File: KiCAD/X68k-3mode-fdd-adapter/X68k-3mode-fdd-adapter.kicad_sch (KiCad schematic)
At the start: 49 parts, among them J1 Conn_02x17_Odd_Even, J2 Double Row 3A Copper Alloy 34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, J3 Conn_01x04, J4 PH-4A, J5 SDIO, J6 Conn_01x04, J7 Conn_01x03_Pin, P1 USB_C_Plug_USB2.0, Q1 2SC2712, SW1 SW_DIP_x02, SW2 SW_SPDT, U1 CH32V003F4U6, U4 74HC153, U5 74HC153, U6 ULN2003A

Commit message: Minyas-XのV2基板の回路図を一通り日いいたので一旦コミット
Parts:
- removed C1: 10uF, Capacitor_SMD:C_0603_1608Metric, symbol Device:C_Small
- removed C2, C3, C4: 0.1uF, Capacitor_SMD:C_0603_1608Metric, symbol Device:C_Small
- removed D1, D2: SK6812MINI, x68k-lib:SK6812MINI-HS, symbol X68k-lib:SK6812MINI-HS
- removed J2: Double Row 3A Copper Alloy 34P Female Headers (PM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, x68k-lib:PinSocket_2x17_P2.54mm_Horizontal_Mirror, symbol Connector_Generic:Conn_02x17_Odd_Even
- removed J3: Conn_01x04, x68k-lib:TE_AMP_171826-4, symbol Connector_Generic:Conn_01x04
- removed J5: SDIO, Connector_PinHeader_2.54mm:PinHeader_1x02_P2.54mm_Vertical, symbol Connector:Conn_01x02_Pin
- removed J7: Conn_01x03_Pin, Connector_PinHeader_2.54mm:PinHeader_1x03_P2.54mm_Vertical, symbol Connector:Conn_01x03_Pin
- removed P1: USB_C_Plug_USB2.0, Connector_USB:USB_C_Receptacle_GCT_USB4125-xx-x-0190_6P_TopMnt_Horizontal, symbol Connector:USB_C_Receptacle_PowerOnly_6P
- removed R0, R1, R10, R11, R12, R13, R2, R3, R5, R6, R7: 1K, Resistor_SMD:R_0603_1608Metric, symbol Device:R_Small_US
- removed R24, R25, R26, R27: 10K, Resistor_SMD:R_0603_1608Metric, symbol Device:R_Small_US
- removed R31, R32: 5.1k, Resistor_SMD:R_0603_1608Metric, symbol Device:R_Small_US
- removed SW2: SW_SPDT, Connector_PinHeader_2.54mm:PinHeader_1x03_P2.54mm_Vertical, symbol Switch:SW_SPDT
- removed TP2, TP4: TestPoint, TestPoint:TestPoint_Pad_1.0x1.0mm, symbol Connector:TestPoint
- removed U1: CH32V003F4U6, Package_DFN_QFN:QFN-20-1EP_3x3mm_P0.4mm_EP1.65x1.65mm_ThermalVias, symbol X68k-lib:CH32V003F4U6
- removed U4, U5: 74HC153, Package_SO:SO-16_5.3x10.2mm_P1.27mm, symbol 74xx_IEEE:74153
- removed U6: ULN2003A, Package_SO:SOP-16_3.9x9.9mm_P1.27mm, symbol Transistor_Array:ULN2003A
- added C101: 0.1uF, symbol Device:C_Small
- added C103, C104, C105, C106, C107: 0.1uF, Capacitor_SMD:C_0603_1608Metric, symbol Device:C_Small
- added J103, J104: Conn_01x02, symbol Connector_Generic:Conn_01x02
- added J106, J109: Conn_02x17_Odd_Even, symbol Connector_Generic:Conn_02x17_Odd_Even
- added JP101: Jumper_NC_Small, Jumper:SolderJumper-2_P1.3mm_Bridged_RoundedPad1.0x1.5mm, symbol device:Jumper_NC_Small
- added JP102, JP103: Jumper_2_Small_Open, symbol Jumper:Jumper_2_Small_Open
- added Q101: DTC143Z, symbol Transistor_BJT:DTC143Z
- added R101, R104: R100 (0.1Ω), Resistor_SMD:R_2512_6332Metric_Pad1.40x3.35mm_HandSolder, symbol Device:R_Small_US
- added R113, R114: 2.2k, symbol Device:R_Small_US
- added R115: 1k, symbol Device:R_Small_US
- added R120, R121, R122, R123, R124, R125, R126, R127, R128, R129, R130, R131, R132, R133, R134, R135, R136, R137: 1K, Resistor_SMD:R_0603_1608Metric, symbol Device:R_Small_US
- added RP101: 4.7k, Resistor_SMD:R_Array_Convex_4x0603, symbol device:R_PACK4
- added SW102: RESET_SW, symbol Switch:SW_Push
- added TP104, TP105, TP106, TP108, TP109, TP110, TP111, TP113, TP114: TestPoint, TestPoint:TestPoint_Pad_1.0x1.0mm, symbol Connector:TestPoint
- added U101: INA3221AIRGVR, Housings_DFN_QFN:QFN-16-1EP_4x4mm_Pitch0.65mm, symbol x68000-ext:INA3221
- added U102, U104, U105: SLG46826G(V2), Package_SO:TSSOP-20_4.4x6.5mm_P0.65mm, symbol X68k-lib:SLG46826G(V2)
- added U103: CH32X035C8T6, Package_LQFP:LQFP-48-1EP_7x7mm_P0.5mm, symbol X68k-lib:CH32X035C8T6
- J102: renamed from J4; value PH-4A -> 4pin
- renumbered BZ1 to BZ101, C5 to C102, D3 to D103, H1 to H101, J6 to J105, J1 to J107, Q1 to Q102, R21 to R102, R20 to R103, R22 to R119, SW1 to SW101, TP3 to TP101, TP1 to TP102
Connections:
- net +5V: no longer C102.1, J102.1 (Pin_1)
- net BUZZER: now also U103.17 (PA7)
- net DIPSW_0: now also U103.40 (PA8)
- net DIPSW_1: now also U103.41 (PA9)
- net DIRECTION: now also R129.2, U103.45 (PA13)
- net DISK_CHANGE_DOSV: now also J106.34 (Pin_34), J109.34 (Pin_34), U103.28 (PB8)
- net DISK_IN: now also U104.5 (IO10)
- net DISK_TYPE_SELECT: no longer TP101.1
- net DRIVE_SELECT_0: now also R120.2, U102.1 (IO14)
- net DRIVE_SELECT_1: now also R121.2, U102.2 (IO13)
- net DRIVE_SELECT_2: now also R122.2, U102.3 (IO12)
- net DRIVE_SELECT_3: now also R123.2, U102.4 (IO11)
- net EJECT: now also R133.2, U103.2 (PA16)
- net EJECT_MASK: now also R134.2, U103.3 (PA17)
- net ERR_DISK: now also U104.6 (IO9)
- net GND: now also C101.2, C103.2, C104.2, C105.2, C106.2, C107.2, J103.2 (Pin_2), J104.2 (Pin_2), J106.11 (Pin_11), J106.13 (Pin_13), J106.15 (Pin_15), J106.17 (Pin_17), J106.19 (Pin_19), J106.21 (Pin_21), J106.23 (Pin_23), J106.25 (Pin_25), J106.27 (Pin_27), J106.29 (Pin_29), J106.31 (Pin_31), J106.33 (Pin_33), J106.5 (Pin_5), J106.7 (Pin_7), J106.9 (Pin_9), J109.11 (Pin_11), J109.13 (Pin_13), J109.15 (Pin_15), J109.17 (Pin_17), J109.19 (Pin_19), J109.21 (Pin_21), J109.23 (Pin_23), J109.25 (Pin_25), J109.27 (Pin_27), J109.29 (Pin_29), J109.31 (Pin_31), J109.33 (Pin_33), J109.5 (Pin_5), J109.7 (Pin_7), J109.9 (Pin_9), JP101.2, Q101.2 (E), SW102.1, U101.17 (PAD), U101.3 (GND), U102.10 (GND), U103.47 (GND), U104.10 (GND)
- net INDEX: now also U105.3 (IO12)
- net LED_BLINK: now also R135.2, U103.4 (PA18)
- net LED_DATA: now also U103.19 (PC7)
- net MODE_SELECT_DOSV: now also J106.2 (Pin_2), J109.2 (Pin_2)
- net MOTOR_ON: now also R128.2, U103.44 (PA12)
- net OPTION_SELECT_0: now also R124.2, U104.1 (IO14)
- net OPTION_SELECT_1: now also R125.2, U104.2 (IO13)
- net OPTION_SELECT_2: now also R126.2, U104.3 (IO12)
- net OPTION_SELECT_3: now also R127.2, U104.4 (IO11)
- net READY: now also U102.5 (IO10)
- net READ_DATA: now also U105.4 (IO11)
- net SIDE_SELECT: now also R131.2, R132.2, U103.1 (PA15)
- net STEP: now also R130.2, U103.46 (PA14)
- net TRACK_00: now also U105.1 (IO14)
- net WRITE_DATA: now also R137.2, U105.6 (IO9)
- net WRITE_GATE: now also R136.2, U105.5 (IO10)
- net WRITE_PROTECT: now also U105.2 (IO13)
- net +12V renamed +12V_FDD
- net +12V_FDD: now also R101.2, U101.14 (IN-2)
- net DRIVE_SELECT_DOSV_0: no longer names the net of TP102.1
- net DRIVE_SELECT_DOSV_0: now also J109.10 (Pin_10)
- net SCL renamed I2C_SCL
- net I2C_SCL: now also R114.2, U101.6 (SCL), U102.13 (SCL), U103.42 (PA10/SCL), U104.13 (SCL), U105.13 (SCL)
- net SDA renamed I2C_SDA
- net I2C_SDA: now also JP102.2 (B), JP103.2 (B), R113.2, U101.7 (SDA), U102.12 (SDA), U103.43 (PA11/SDA)
- new net: JP103.1 (A), U105.12 (SDA)
- new net: TP113.1, U105.8 (IO8)
- new net: TP114.1, U105.9 (IO7)
- new net: RP101.2 (P2), U101.10 (PV)
- new net: RP101.1 (P1), U101.13 (TC)
- new net: JP101.1, U101.5 (A0)
- new net: RP101.4 (P4), U101.8 (WARN)
- new net: RP101.3 (P3), U101.9 (CRIT)
- new net: JP102.1 (A), U104.12 (SDA)
- new net: R115.2, SW102.2, U103.7 (PA21)
- new net: J106.10 (Pin_10), TP111.1
- new net: TP108.1, U104.18 (IO1)
- new net: TP109.1, U104.11 (IO6)
- new net: TP110.1, U104.9 (IO7)
- new net: TP105.1, U102.11 (IO6)
- new net: TP101.1, U102.6 (IO9)
- new net: TP104.1, U102.8 (IO8)
- new net: TP106.1, U102.9 (IO7)
- new net: J104.1 (Pin_1), Q101.1 (B)
- new net +12V_ENABLE_n: U103.8 (PA22)
- new net +12V_EXT_DET_n: U102.16 (IO3)
- new net +12V_EXT_ENABLE_n: U103.9 (PA23)
- new net +12V_FDD_S: R101.1, U101.15 (IN+2)
- new net +12V_REQUEST: U102.18 (IO1)
- new net +5V_ENABLE_n: U103.6 (PA20)
- new net +5V_FDD: J102.1 (Pin_1), R104.2, U101.1 (IN-3)
- new net +5V_FDD_S: R104.1, U101.2 (IN+3)
- new net CC1: U103.38 (PC14/CC1)
- new net CC2: U103.39 (PC15/CC2)
- new net DIRECTION_DOSV: J106.18 (Pin_18), J109.18 (Pin_18), U103.25 (PB5)
- new net DISK_IN_MCU_A: U104.17 (IO2)
- new net DISK_IN_MCU_B: U104.16 (IO3)
- new net DRIVE_SELECT_A: U102.15 (IO4), U103.10 (PA0)
- new net DRIVE_SELECT_B: U102.14 (IO5), U103.11 (PA1)
- new net DRIVE_SELECT_DOSV_1_A: J109.12 (Pin_12)
- new net DRIVE_SELECT_DOSV_1_B: J106.12 (Pin_12)
- new net DRIVE_SELECT_DOSV_A_MCU: U103.22 (PB2)
- new net DRIVE_SELECT_DOSV_B_MCU: U103.23 (PB3)
- new net FDD_INT: U104.8 (IO8)
- new net GP_ENABLE: U102.19 (IO0), U103.37 (PC19/DCK), U104.19 (IO0), U105.19 (IO0)
- new net INDEX_DOSV: J106.8 (Pin_8), J109.8 (Pin_8), U103.16 (PA6), U105.16 (IO3)
- new net IN_USE_DOSV: J106.4 (Pin_4), J109.4 (Pin_4), U103.21 (PB1)
- new net MODE_SELECT_DOSV_MCU: U103.20 (PB0)
- new net MOTOR_ON_DOSV: J106.16 (Pin_16), J109.16 (Pin_16), U103.24 (PB4)
- new net OPTION_SELECT_A: U103.12 (PA2), U104.15 (IO4)
- new net OPTION_SELECT_B: U103.13 (PA3), U104.14 (IO5)
- new net READY_MCU_A: U103.35 (PB12)
- new net READY_MCU_B: U103.36 (PB13)
- new net READ_DATA_DOSV: J106.30 (Pin_30), J109.30 (Pin_30), U103.29 (PB9), U105.15 (IO4)
- new net SIDE_SELECT_DOSV: J106.32 (Pin_32), J109.32 (Pin_32)
- new net SIDE_SELECT_MCU: U103.27 (PB7)
- new net STEP_DOSV: J106.20 (Pin_20), J109.20 (Pin_20), U103.26 (PB6)
- new net TRACK00_DOSV: U103.30 (PB10)
- new net TRACK_00_DOSV: J106.26 (Pin_26), J109.26 (Pin_26), U105.18 (IO1)
- new net USB_D+: U103.33 (PC10/PC17/UDP)
- new net USB_D-: U103.32 (PC11/PC16/UDM)
- new net VBUS: U101.11 (IN-1)
- new net VBUS_S: U101.12 (IN+1)
- new net VCDD_FDDIF: R120.1, R121.1, R122.1, R123.1, R124.1, R125.1, R126.1, R127.1, R128.1, R129.1, R130.1, R131.1, R132.1, R133.1, R134.1, R135.1, R136.1, R137.1
- new net VDD_FDDIF: C103.1, C104.1, C106.1, U102.7 (V_{DD2}), U104.7 (V_{DD2})
- new net VDD_MCU: C101.1, C102.1, C105.1, C107.1, R113.1, R114.1, R115.1, RP101.5 (R4), RP101.6 (R3), RP101.7 (R2), RP101.8 (R1), U101.16 (VPU), U101.4 (VS), U102.20 (V_{DD}), U103.48 (VDD), U104.20 (V_{DD})
- new net WRITE_DATA_DOSV: J106.22 (Pin_22), J109.22 (Pin_22), U105.11 (IO6)
- new net WRITE_GATE_DOSV: J106.24 (Pin_24), J109.24 (Pin_24), U105.14 (IO5)
- new net WRITE_PROTECT_DOSV: J106.28 (Pin_28), J109.28 (Pin_28), U105.17 (IO2)
- new net X68K_PWR: U102.17 (IO2)
- new net X68k_PWR: J103.1 (Pin_1), Q101.3 (C)
- no-connect marks 12 -> 9
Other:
- added sheet SerialLEDs (serial_leds.kicad_sch)
- added sheet USB-PD-PWR (usb_pd_pwr.kicad_sch)
- added sheet open_drain_buffer (open_drain_buffer.kicad_sch)
- added sheet open_drain_buffer1 (open_drain_buffer.kicad_sch)
- added sheet open_drain_buffer2 (open_drain_buffer.kicad_sch)
- added sheet open_drain_buffer3 (open_drain_buffer.kicad_sch)
- added sheet open_drain_buffer4 (open_drain_buffer.kicad_sch)
- added sheet open_drain_buffer5 (open_drain_buffer.kicad_sch)
- added sheet open_drain_buffer6 (open_drain_buffer.kicad_sch)
- added sheet open_drain_buffer7 (open_drain_buffer.kicad_sch)
- moved on the sheet: BZ101, C102, D103, H101, J105, J107, Q102, R102, R103, R119, SW101, TP101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

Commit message: DRCエラー修正
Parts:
- removed JP101: Jumper_NC_Small, Jumper:SolderJumper-2_P1.3mm_Bridged_RoundedPad1.0x1.5mm, symbol device:Jumper_NC_Small
- removed RP101: 4.7k, Resistor_SMD:R_Array_Convex_4x0603, symbol device:R_PACK4
- removed SW101: SW_DIP_x02, Button_Switch_SMD:SW_DIP_SPSTx02_Slide_Copal_CHS-02B_W7.62mm_P1.27mm, symbol Switch:SW_DIP_x02
- removed TP108: TestPoint, TestPoint:TestPoint_Pad_1.0x1.0mm, symbol Connector:TestPoint
- added H102, H103, H104: MountingHole_Pad, MountingHole:MountingHole_2.7mm_M2.5_Pad, symbol Mechanical:MountingHole_Pad
- added J108: Conn_02x06_Odd_Even, symbol Connector_Generic:Conn_02x06_Odd_Even
- added JP101: Jumper_2_Small_Bridged, symbol Jumper:Jumper_2_Small_Bridged
- added R102, R103: 10K, Resistor_SMD:R_0603_1608Metric, symbol Device:R_Small_US
- added R129: 1K, Resistor_SMD:R_0603_1608Metric, symbol Device:R_Small_US
- added RN101: 4.7k, symbol Device:R_Pack04
- added SW101: SW_DIP_x04, symbol Switch:SW_DIP_x04
- added TP111: TestPoint, TestPoint:TestPoint_Pad_1.0x1.0mm, symbol Connector:TestPoint
- Q102: footprint Package_TO_SOT_SMD:SOT-23 -> Package_TO_SOT_SMD:SOT-323_SC-70
- U101: footprint Housings_DFN_QFN:QFN-16-1EP_4x4mm_Pitch0.65mm -> Package_DFN_QFN:QFN-16-1EP_4x4mm_P0.65mm_EP2.1x2.1mm_ThermalVias
- U102, U105: symbol X68k-lib:SLG46826G(V2) -> x68000-ext:SLG46826G(V2)
- U103: renamed from U104; symbol X68k-lib:SLG46826G(V2) -> x68000-ext:SLG46826G(V2)
- U104: renamed from U103; footprint Package_LQFP:LQFP-48-1EP_7x7mm_P0.5mm -> Package_QFP:LQFP-48-1EP_7x7mm_P0.5mm_EP3.6x3.6mm_ThermalVias; symbol X68k-lib:CH32X035C8T6 -> x68000-ext:CH32X035C8T6
- renumbered C103 to C101, C104 to C103, C105 to C104, C101 to C105, D103 to D101, J102 to J101, J103 to J102, J105 to J103, J109 to J105, J107 to J106, J106 to J107, R102 to R104, R103 to R105, R104 to R106, R119 to R107, R120 to R108, R121 to R109, R122 to R110, R123 to R111, R124 to R112, R125 to R113, R126 to R114, R127 to R115, R113 to R116, R114 to R117, R128 to R118, R129 to R119, R130 to R120, R131 to R121, R132 to R122, R133 to R123, R134 to R124, R135 to R125, R136 to R126, R137 to R127, R115 to R128, TP102 to TP101, TP101 to TP102, TP104 to TP103, TP105 to TP104, TP106 to TP105, TP109 to TP106, TP111 to TP107, TP110 to TP108, TP113 to TP109, TP114 to TP110
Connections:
- net +12V_EXT_DET_n is gone; now on net READY_MCU_B: U102.16 (IO3)
- net +5V is gone; now on net VDD_MCU: BZ101.1, D101.1 (K), J103.2 (Pin_2)
- net FDD_INT_BUF is gone; now on net FDD_INT: J106.19 (Pin_19)
- net TRACK00_DOSV is gone; now on net TRACK_00_DOSV: U104.30 (PB10)
- net VCDD_FDDIF is gone; now on net VDD_FDDIF: R108.1, R109.1, R110.1, R111.1, R112.1, R113.1, R114.1, R115.1, R118.1, R119.1, R120.1, R121.1, R122.1, R123.1, R124.1, R125.1, R126.1, R127.1
- net X68K_PWR is gone; now on net READY_MCU_A: U102.17 (IO2)
- net +12V_ENABLE_n: now also U104.5 (PA19); no longer U104.8 (PA22)
- net +12V_EXT_DET: now also U104.3 (PA17)
- net +12V_EXT_ENABLE_n: now also U104.6 (PA20); no longer U104.9 (PA23)
- net +5V_ENABLE_n: now also U104.4 (PA18); no longer U104.6 (PA20)
- net DIRECTION_DOSV: no longer U104.25 (PB5)
- net DISK_TYPE_SELECT: now also U104.41 (PA9), R129.2
- net EJECT: now also U104.14 (PA4); no longer U104.2 (PA16)
- net EJECT_MASK: now also U104.15 (PA5); no longer U104.3 (PA17)
- net GND: now also U105.10 (GND), H102.1, H103.1, H104.1, J108.10 (Pin_10), J108.12 (Pin_12), J108.2 (Pin_2), J108.4 (Pin_4), J108.6 (Pin_6), J108.8 (Pin_8), JP101.2 (B), R102.2, R103.2
- net I2C_SCL: now also J108.9 (Pin_9)
- net I2C_SDA: now also J108.11 (Pin_11)
- net IN_USE_DOSV: no longer U104.21 (PB1)
- net IN_USE_DOSV_MCU: now also U104.21 (PB1)
- net LED_BLINK: now also U104.40 (PA8); no longer U104.4 (PA18)
- net LED_DATA: now also J108.7 (Pin_7)
- net MOTOR_ON_DOSV: no longer U104.24 (PB4)
- net STEP_DOSV: no longer U104.26 (PB6)
- net VDD_FDDIF: now also U105.7 (V_{DD2}), J108.3 (Pin_3), R129.1
- net VDD_MCU: now also U105.20 (V_{DD}), J108.1 (Pin_1), RN101.5 (R4.2), RN101.6 (R3.2), RN101.7 (R2.2), RN101.8 (R1.2), SW101.5, SW101.6, SW101.7, SW101.8
- net X68k_PWR: now also U104.2 (PA16)
- net at U101.10 (PV): now also RN101.2 (R2.1)
- net at U101.13 (TC): now also RN101.1 (R1.1)
- net at U101.5 (A0): now also JP101.1 (A)
- net at U101.8 (WARN): now also RN101.4 (R4.1)
- net at U101.9 (CRIT): now also RN101.3 (R3.1)
- net CONTROLLER_OPTION: now reaches U104.34 (PC18/DIO)
- net CONTROLLER_OPTION: now also J108.5 (Pin_5)
- net DIPSW_MODESEL_POL: now reaches U103.18 (IO1)
- net DIPSW_MODESEL_POL: now also R104.1, R105.1, SW101.3
- net +12V_REQUEST: no longer names the net of U102.18 (IO1)
- net +12V_REQUEST: now also TP111.1
- removed net DIPSW_0: R105.1, U104.40 (PA8)
- removed net DIPSW_1: R104.1, U104.41 (PA9)
- net DISK_IN_MCU_A renamed DIPSW_12V_REQ
- net DIPSW_12V_REQ: now also SW101.4
- net DISK_IN_MCU_B: no longer names the net of U103.16 (IO3)
- new net DIPSW_DS0: R102.1, SW101.1, U104.8 (PA22)
- new net DIPSW_DS1: R103.1, SW101.2, U104.9 (PA23)
- new net DIRECTION_DOSV_MCU: U104.25 (PB5)
- new net MOTOR_ON_DOSV_MCU: U104.24 (PB4)
- new net STEP_DOSV_MCU: U104.26 (PB6)
- no-connect marks 9 -> 12
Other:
- sheet USB-PD-PWR ports: added USB_D+, USB_D-; removed none
- moved on the sheet: BZ101, C106, C107, D101, JP103, R104, R105, R107, R116, R117, TP109, TP110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

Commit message: アノテーション再実施
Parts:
- renumbered J108 to J102, J102 to J103, J103 to J104, J104 to J105, J105 to J106, J106 to J107, J107 to J108, R129 to R108, R108 to R109, R109 to R110, R110 to R111, R111 to R112, R112 to R113, R113 to R114, R114 to R115, R115 to R116, R116 to R117, R117 to R118, R118 to R119, R119 to R120, R120 to R121, R121 to R122, R122 to R123, R123 to R124, R124 to R125, R125 to R126, R126 to R127, R127 to R128, R128 to R129, TP111 to TP101, TP101 to TP102, TP102 to TP103, TP103 to TP104, TP104 to TP105, TP105 to TP106, TP106 to TP107, TP107 to TP108, TP108 to TP109, TP109 to TP110, TP110 to TP111

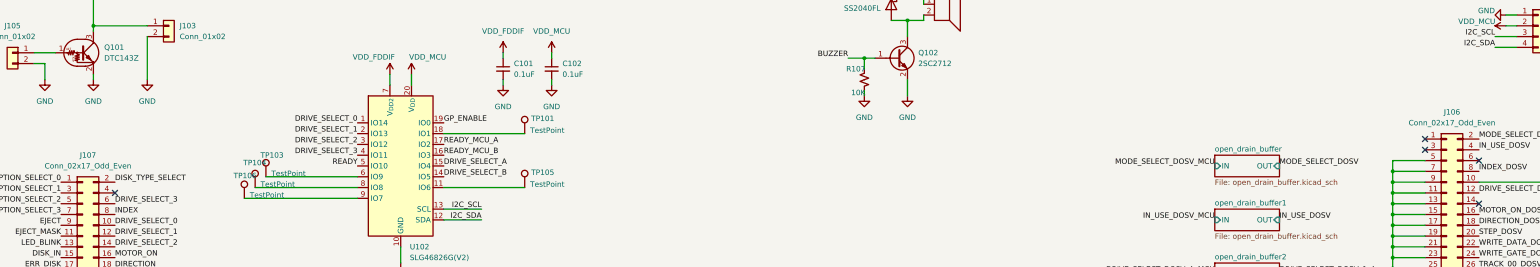
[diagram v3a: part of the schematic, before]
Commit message: フットプリントを一通り割り当てた
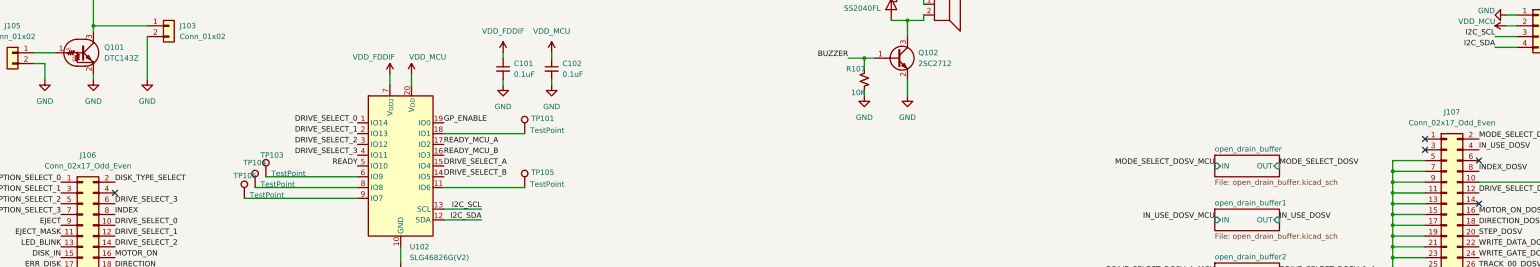
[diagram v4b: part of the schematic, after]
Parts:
- C105: footprint (none) -> Capacitor_SMD:C_0603_1608Metric
- J102: footprint (none) -> Connector_PinSocket_2.54mm:PinSocket_2x06_P2.54mm_Horizontal
- J103: footprint (none) -> Connector_PinHeader_2.54mm:PinHeader_1x02_P2.54mm_Vertical
- J105: footprint (none) -> Connector_JST:JST_VH_B2P-VH-FB-B_1x02_P3.96mm_Vertical
- J107: renamed from J106; footprint (none) -> Connector_IDC:IDC-Header_2x17_P2.54mm_Vertical
- J108: footprint (none) -> Connector_IDC:IDC-Header_2x17_P2.54mm_Vertical
- JP101: footprint (none) -> Jumper:SolderJumper-2_P1.3mm_Bridged_RoundedPad1.0x1.5mm
- JP102, JP103: footprint (none) -> Jumper:SolderJumper-2_P1.3mm_Open_RoundedPad1.0x1.5mm
- Q101: footprint (none) -> Package_TO_SOT_SMD:SOT-523; LCSC (none) -> C5273798
- R117, R118, R129, RN101: footprint (none) -> Resistor_SMD:R_0603_1608Metric
- SW101: footprint (none) -> Button_Switch_SMD:SW_DIP_SPSTx04_Slide_Copal_CHS-04B_W7.62mm_P1.27mm; LCSC (none) -> C319050
- SW102: footprint (none) -> Button_Switch_SMD:SW_Push_SPST_NO_Alps_SKRK
- renumbered J107 to J106
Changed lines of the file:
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@@
 			)
 		)
-		(property "Footprint" ""
+		(property "Footprint" "Jumper:SolderJumper-2_P1.3mm_Open_RoundedPad1.0x1.5mm"
 			(at 138.43 203.2 0)
 			(effects
@@
 			)
 		)
-		(property "Footprint" ""
+		(property "Footprint" "Resistor_SMD:R_0603_1608Metric"
 			(at 193.04 218.44 0)
 			(effects
@@
 			)
 		)
-		(property "Footprint" ""
+		(property "Footprint" "Resistor_SMD:R_0603_1608Metric"
 			(at 200.66 218.44 0)
 			(effects
@@
 			)
 		)
-		(property "Footprint" ""
+		(property "Footprint" "Connector_PinHeader_2.54mm:PinHeader_1x02_P2.54mm_Vertical"
 			(at 69.85 100.33 0)
 			(effects
@@
 			)
 		)
-		(property "Footprint" ""
+		(property "Footprint" "Jumper:SolderJumper-2_P1.3mm_Bridged_RoundedPad1.0x1.5mm"
 			(at 187.96 44.45 0)
 			(effects
@@
 			)
 		)
-		(property "Footprint" ""
+		(property "Footprint" "Jumper:SolderJumper-2_P1.3mm_Open_RoundedPad1.0x1.5mm"
 			(at 138.43 260.35 0)
 			(effects
@@
 			)
 		)
-		(property "Footprint" ""
+		(property "Footprint" "Package_TO_SOT_SMD:SOT-523"
 			(at 49.53 106.68 0)
 			(effects
@@
 			)
 		)
+		(property "LCSC" "C5273798"
+			(at 49.53 106.68 0)
+			(effects
+				(font
+					(size 1.27 1.27)
+				)
+				(hide yes)
+			)
+		)
 		(pin "2"
 		)
@@
 			)
 		)
-		(property "Footprint" ""
+		(property "Footprint" "Connector_JST:JST_VH_B2P-VH-FB-B_1x02_P3.96mm_Vertical"
 			(at 33.02 106.68 0)
 			(effects
@@
 		(dnp no)
 		(fields_autoplaced yes)
-		(property "Reference" "J107"
+		(property "Reference" "J106"
 			(at 50.8 130.81 0)
 			(effects
@@
 			(project ""
 				(path "/13b3a4ee-84d6-44b3-962d-9cf7c36d7564"
-					(reference "J107")
+					(reference "J106")
 					(unit 1)
 				)
@@
 			)
 		)
-		(property "Footprint" ""
+		(property "Footprint" "Button_Switch_SMD:SW_DIP_SPSTx04_Slide_Copal_CHS-04B_W7.62mm_P1.27mm"
 			(at 259.08 55.88 0)
 			(effects
@@
 			)
 		)
+		(property "LCSC" "C319050"
+			(at 259.08 55.88 0)
+			(effects
+				(font
+					(size 1.27 1.27)
+				)
+				(hide yes)
+			)
+		)
 		(pin "3"
 		)
@@
 			)
 		)
-		(property "Footprint" ""
+		(property "Footprint" "Capacitor_SMD:C_0603_1608Metric"
 			(at 264.16 181.61 0)
 			(effects
@@
 			)
 		)
-		(property "Footprint" ""
+		(property "Footprint" "Connector_IDC:IDC-Header_2x17_P2.54mm_Vertical"
 			(at 370.84 209.55 0)
 			(effects
@@
 			)
 		)
-		(property "Footprint" ""
+		(property "Footprint" "Connector_PinSocket_2.54mm:PinSocket_2x06_P2.54mm_Horizontal"
 			(at 370.84 68.58 0)
 			(effects
@@
 			)
 		)
-		(property "Footprint" ""
+		(property "Footprint" "Button_Switch_SMD:SW_Push_SPST_NO_Alps_SKRK"
 			(at 189.23 257.81 0)
 			(effects
@@
 			)
 		)
-		(property "Footprint" ""
+		(property "Footprint" "Resistor_SMD:R_0603_1608Metric"
 			(at 194.31 248.92 0)
 			(effects
@@
 		(dnp no)
 		(fields_autoplaced yes)
-		(property "Reference" "J106"
+		(property "Reference" "J107"
 			(at 372.11 120.65 0)
 			(effects
@@
 			)
 		)
-		(property "Footprint" ""
+		(property "Footprint" "Connector_IDC:IDC-Header_2x17_P2.54mm_Vertical"
 			(at 370.84 147.32 0)
 			(effects
@@
 			(project ""
 				(path "/13b3a4ee-84d6-44b3-962d-9cf7c36d7564"
-					(reference "J106")
+					(reference "J107")
 					(unit 1)
 				)
@@
 			)
 		)
-		(property "Footprint" ""
+		(property "Footprint" "Resistor_SMD:R_0603_1608Metric"
 			(at 191.77 67.945 90)
 			(effects

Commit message: PCBの配線完了
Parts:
- removed R123: 1K, Resistor_SMD:R_0603_1608Metric, symbol Device:R_Small_US
- added H105: MountingHole_Pad, x68k-lib:PCB_WeldingTerminal_M3_L-angle_PCB-54L, symbol Mechanical:MountingHole_Pad
- added H106: MountingHole_Pad, x68k-lib:PCB_WeldingTerminal_M3_L-angle_PCB-54R, symbol Mechanical:MountingHole_Pad
- H101, H102, H103, H104: footprint MountingHole:MountingHole_2.7mm_M2.5_Pad -> x68k-lib:PCB_WeldingTerminal_M3_L-angle; LCSC (none) -> C962334
- J101: footprint Connector_JST:JST_PH_B4B-PH-K_1x04_P2.00mm_Vertical -> TerminalBlock_Phoenix:TerminalBlock_Phoenix_MPT-0,5-4-2.54_1x04_P2.54mm_Horizontal; LCSC C2321 -> C2927505
- J107, J108: footprint Connector_IDC:IDC-Header_2x17_P2.54mm_Vertical -> Connector_PinHeader_2.54mm:PinHeader_2x17_P2.54mm_Horizontal
- RN101: value 4.7k -> 4.7k x4; footprint Resistor_SMD:R_0603_1608Metric -> Resistor_SMD:R_Array_Concave_4x0603; LCSC (none) -> C1980
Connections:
- net +12V_FDD: now also J101.1 (Pin_1); no longer J101.4 (Pin_4)
- net +5V_FDD: now also J101.4 (Pin_4); no longer J101.1 (Pin_1)
- net DIPSW_12V_REQ: now also R105.1
- net DIPSW_MODESEL_POL: no longer R105.1
- net GND: now also H105.1, H106.1
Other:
- moved on the sheet: J104

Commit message: 基板の外径を変更して、底面部のネジ穴に合うホールを追加
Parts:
- added H107, H108, H109, H110: MountingHole_Pad, MountingHole:MountingHole_3.2mm_M3_ISO14580_Pad, symbol Mechanical:MountingHole_Pad
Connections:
- net GND: now also H107.1, H108.1, H109.1, H110.1
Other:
- moved on the sheet: H101, H102, H103, H104

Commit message: 部品の配置、シルクを調整
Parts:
- H107, H108, H109, H110: footprint MountingHole:MountingHole_3.2mm_M3_ISO14580_Pad -> x68k-lib:MountingHole_3.2mm_M3_Pad_Small
- J105: footprint Connector_JST:JST_VH_B2P-VH-FB-B_1x02_P3.96mm_Vertical -> Connector_JST:JST_XH_S2B-XH-A_1x02_P2.50mm_Horizontal
- SW102: value RESET_SW -> RESET
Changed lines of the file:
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@@
 			)
 		)
-		(property "Footprint" "MountingHole:MountingHole_3.2mm_M3_ISO14580_Pad"
+		(property "Footprint" "x68k-lib:MountingHole_3.2mm_M3_Pad_Small"
 			(at 304.8 41.91 0)
 			(effects
@@
 			)
 		)
-		(property "Footprint" "MountingHole:MountingHole_3.2mm_M3_ISO14580_Pad"
+		(property "Footprint" "x68k-lib:MountingHole_3.2mm_M3_Pad_Small"
 			(at 325.12 41.91 0)
 			(effects
@@
 			)
 		)
-		(property "Footprint" "Connector_JST:JST_VH_B2P-VH-FB-B_1x02_P3.96mm_Vertical"
+		(property "Footprint" "Connector_JST:JST_XH_S2B-XH-A_1x02_P2.50mm_Horizontal"
 			(at 33.02 106.68 0)
 			(effects
@@
 			)
 		)
-		(property "Value" "RESET_SW"
+		(property "Value" "RESET"
 			(at 195.58 259.0799 90)
 			(effects
@@
 			)
 		)
-		(property "Footprint" "MountingHole:MountingHole_3.2mm_M3_ISO14580_Pad"
+		(property "Footprint" "x68k-lib:MountingHole_3.2mm_M3_Pad_Small"
 			(at 294.64 41.91 0)
 			(effects
@@
 			)
 		)
-		(property "Footprint" "MountingHole:MountingHole_3.2mm_M3_ISO14580_Pad"
+		(property "Footprint" "x68k-lib:MountingHole_3.2mm_M3_Pad_Small"
 			(at 314.96 41.91 0)
 			(effects
